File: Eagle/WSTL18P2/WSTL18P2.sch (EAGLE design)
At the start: 22 parts, among them CON1 1X6CONN-1.27-ROUND, CON2 1X6CONN-1.27-ROUND, CON3 1X6CONN-1.27-ROUND, CON4 1X6CONN-1.27-ROUND, T1 ABS07AIG

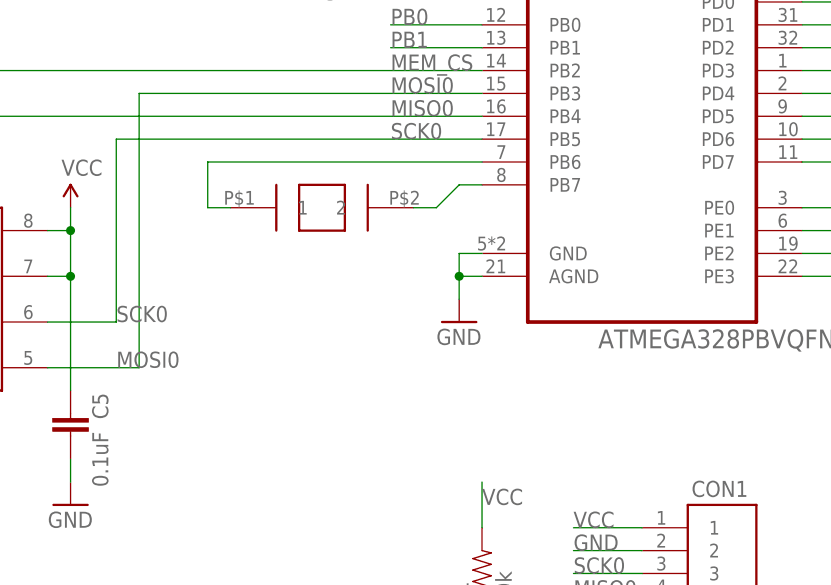
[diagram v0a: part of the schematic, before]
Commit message: Reverted some passives back to 0402 size
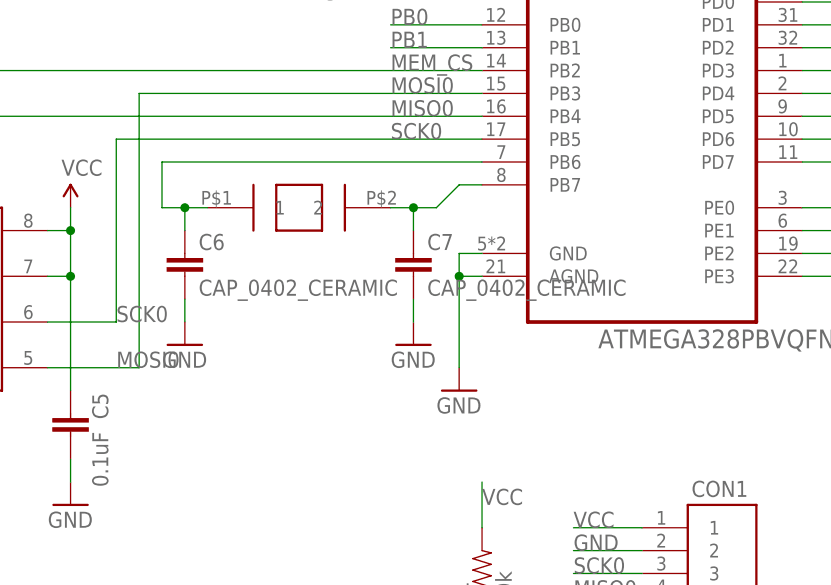
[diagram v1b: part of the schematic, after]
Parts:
- added C6, C7: CAP_0402_CERAMIC, Passives:CAP_0402_CERAMIC
- C4, C5: device Passives:CAP_0201_CERAMIC -> Passives:CAP_0402_CERAMIC
- R1, R2, R3, R4, R5: device Passives:RES_0201_CERAMIC -> Passives:RES_0402_CERAMIC
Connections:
- net GND: now also C6.2, C7.2
- net N$1: now also C7.1
- net N$2: now also C6.1
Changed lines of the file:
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@@
 <part name="GND4" library="SparkFun-Aesthetics" deviceset="GND" device=""/>
 <part name="MEM" library="Memory" deviceset="AT25DN512C-XMHF-B" device=""/>
-<part name="C4" library="Passives" deviceset="CAP_0201_CERAMIC" device="" value="0.1uF"/>
-<part name="C5" library="Passives" deviceset="CAP_0201_CERAMIC" device="" value="0.1uF"/>
+<part name="C4" library="Passives" deviceset="CAP_0402_CERAMIC" device="" value="0.1uF"/>
+<part name="C5" library="Passives" deviceset="CAP_0402_CERAMIC" device="" value="0.1uF"/>
 <part name="GND2" library="SparkFun-Aesthetics" deviceset="GND" device=""/>
 <part name="GND5" library="SparkFun-Aesthetics" deviceset="GND" device=""/>
 <part name="GND6" library="SparkFun-Aesthetics" deviceset="GND" device=""/>
 <part name="GND7" library="SparkFun-Aesthetics" deviceset="GND" device=""/>
-<part name="R2" library="Passives" deviceset="RES_0201_CERAMIC" device="" value="4.7k"/>
-<part name="R3" library="Passives" deviceset="RES_0201_CERAMIC" device="" value="4.7k"/>
-<part name="R1" library="Passives" deviceset="RES_0201_CERAMIC" device="" value="10k"/>
+<part name="R2" library="Passives" deviceset="RES_0402_CERAMIC" device="" value="4.7k"/>
+<part name="R3" library="Passives" deviceset="RES_0402_CERAMIC" device="" value="4.7k"/>
+<part name="R1" library="Passives" deviceset="RES_0402_CERAMIC" device="" value="10k"/>
 <part name="LED0" library="Passives" deviceset="LED_0402" device=""/>
 <part name="GND8" library="SparkFun-Aesthetics" deviceset="GND" device=""/>
-<part name="R5" library="Passives" deviceset="RES_0201_CERAMIC" device="" value="1k"/>
-<part name="R4" library="Passives" deviceset="RES_0201_CERAMIC" device="" value="4.7k"/>
+<part name="R5" library="Passives" deviceset="RES_0402_CERAMIC" device="" value="1k"/>
+<part name="R4" library="Passives" deviceset="RES_0402_CERAMIC" device="" value="4.7k"/>
 <part name="CON1" library="AVR_ISP_127" deviceset="1X6CONN-1.27-ROUND" device=""/>
 <part name="CON2" library="AVR_ISP_127" deviceset="1X6CONN-1.27-ROUND" device=""/>
@@
 <part name="U$1" library="Battery_holders" deviceset="LINX-CR2032-BAT-HLD-M-THM" device=""/>
 <part name="TWI" library="AVR_ISP_127" deviceset="1X2CONN1.27" device=""/>
+<part name="C6" library="Passives" deviceset="CAP_0402_CERAMIC" device=""/>
+<part name="C7" library="Passives" deviceset="CAP_0402_CERAMIC" device=""/>
+<part name="GND10" library="SparkFun-Aesthetics" deviceset="GND" device=""/>
+<part name="GND12" library="SparkFun-Aesthetics" deviceset="GND" device=""/>
 </parts>
 <sheets>
@@
 <instances>
 <instance part="MCU" gate="A" x="68.58" y="48.26"/>
-<instance part="T1" gate="G$1" x="33.02" y="27.94" smashed="yes" rot="R90"/>
+<instance part="T1" gate="G$1" x="30.48" y="27.94" smashed="yes" rot="R90"/>
 <instance part="C1" gate="G$1" x="43.18" y="71.12" smashed="yes" rot="R270">
 <attribute name="NAME" x="39.116" y="72.517" size="1.778" layer="95" align="center"/>
@@
 <instance part="GND5" gate="1" x="5.08" y="-5.08"/>
 <instance part="GND6" gate="1" x="195.58" y="45.72"/>
-<instance part="GND7" gate="1" x="48.26" y="15.24"/>
+<instance part="GND7" gate="1" x="48.26" y="7.62"/>
 <instance part="R2" gate="G$1" x="139.7" y="68.58" smashed="yes" rot="R90">
 <attribute name="NAME" x="138.2014" y="64.77" size="1.778" layer="95" rot="R90"/>
@@
 <instance part="U$1" gate="G$1" x="-76.2" y="58.42"/>
 <instance part="TWI" gate="G$1" x="127" y="78.74" rot="R90"/>
+<instance part="C6" gate="G$1" x="17.78" y="22.86"/>
+<instance part="C7" gate="G$1" x="43.18" y="22.86"/>
+<instance part="GND10" gate="1" x="43.18" y="12.7"/>
+<instance part="GND12" gate="1" x="17.78" y="12.7"/>
 </instances>
 <busses>
@@
 <pinref part="T1" gate="G$1" pin="2"/>
 <wire x1="45.72" y1="27.94" x2="43.18" y2="27.94" width="0.1524" layer="91"/>
+<pinref part="C7" gate="G$1" pin="1"/>
+<wire x1="43.18" y1="27.94" x2="40.64" y2="27.94" width="0.1524" layer="91"/>
+<wire x1="43.18" y1="25.4" x2="43.18" y2="27.94" width="0.1524" layer="91"/>
+<junction x="43.18" y="27.94"/>
 </segment>
 </net>
@@
 <pinref part="MCU" gate="A" pin="PB6"/>
 <pinref part="T1" gate="G$1" pin="1"/>
-<wire x1="50.8" y1="33.02" x2="20.32" y2="33.02" width="0.1524" layer="91"/>
-<wire x1="20.32" y1="33.02" x2="20.32" y2="27.94" width="0.1524" layer="91"/>
-<wire x1="20.32" y1="27.94" x2="22.86" y2="27.94" width="0.1524" layer="91"/>
+<wire x1="50.8" y1="33.02" x2="15.24" y2="33.02" width="0.1524" layer="91"/>
+<wire x1="15.24" y1="33.02" x2="15.24" y2="27.94" width="0.1524" layer="91"/>
+<wire x1="15.24" y1="27.94" x2="17.78" y2="27.94" width="0.1524" layer="91"/>
+<pinref part="C6" gate="G$1" pin="1"/>
+<wire x1="17.78" y1="27.94" x2="20.32" y2="27.94" width="0.1524" layer="91"/>
+<wire x1="17.78" y1="25.4" x2="17.78" y2="27.94" width="0.1524" layer="91"/>
+<junction x="17.78" y="27.94"/>
 </segment>
 </net>
@@
 <segment>
 <pinref part="GND7" gate="1" pin="GND"/>
-<wire x1="48.26" y1="17.78" x2="48.26" y2="20.32" width="0.1524" layer="91"/>
+<wire x1="48.26" y1="10.16" x2="48.26" y2="20.32" width="0.1524" layer="91"/>
 <pinref part="MCU" gate="A" pin="AGND"/>
 <wire x1="48.26" y1="20.32" x2="50.8" y2="20.32" width="0.1524" layer="91"/>
@@
 <wire x1="116.84" y1="45.72" x2="119.38" y2="45.72" width="0.1524" layer="91"/>
 </segment>
-</net>
+<segment>
+<pinref part="GND12" gate="1" pin="GND"/>
+<pinref part="C6" gate="G$1" pin="2"/>
+<wire x1="17.78" y1="15.24" x2="17.78" y2="17.78" width="0.1524" layer="91"/>
+</segment>
+<segment>
+<pinref part="GND10" gate="1" pin="GND"/>
+<pinref part="C7" gate="G$1" pin="2"/>
+<wire x1="43.18" y1="15.24" x2="43.18" y2="17.78" width="0.1524" layer="91"/>
+</segment>
+</net>

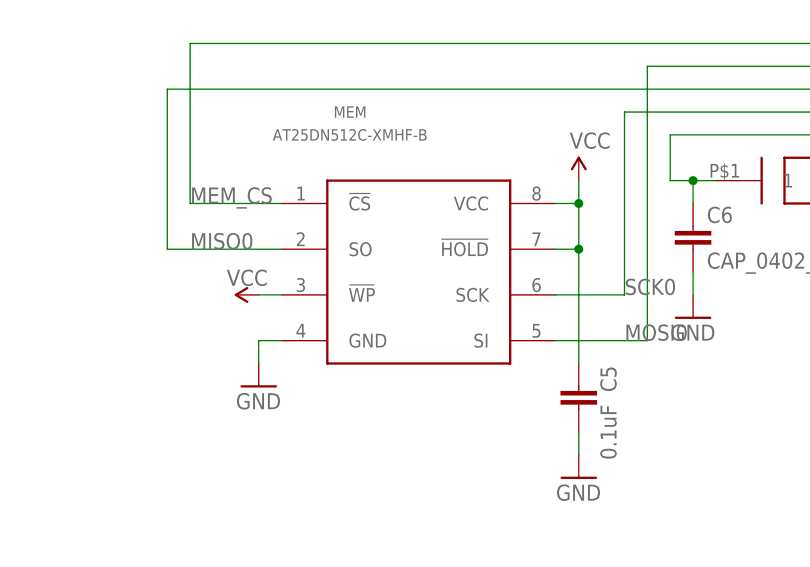
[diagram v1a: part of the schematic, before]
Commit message: Removed WP and HOLD connections to VCC on EEPROM
Chip has internal pull-ups for when WP and HOLD functions are not used
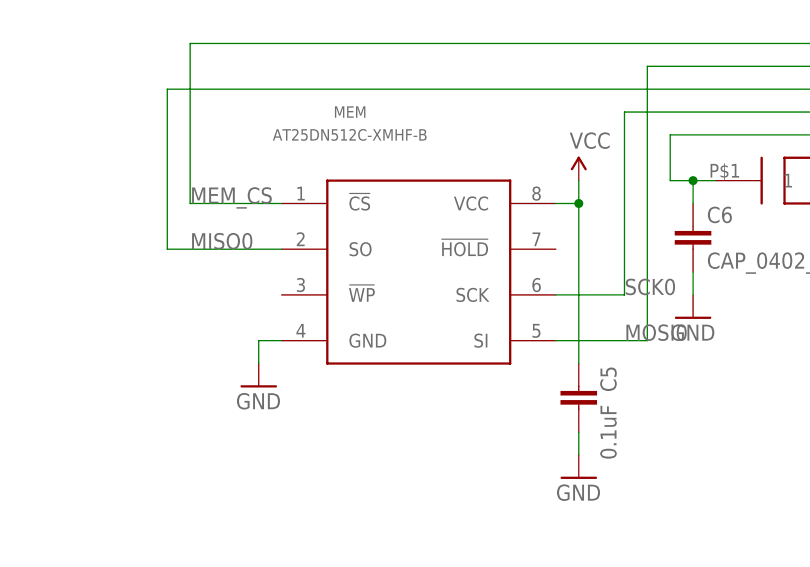
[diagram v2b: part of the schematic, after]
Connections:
- net VCC: no longer MEM.!HOLD!, MEM.!WP!
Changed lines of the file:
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@@
 <part name="GND11" library="SparkFun-Aesthetics" deviceset="GND" device=""/>
 <part name="VCC5" library="SparkFun-Aesthetics" deviceset="5V" device="" value="VCC"/>
-<part name="VCC6" library="SparkFun-Aesthetics" deviceset="5V" device="" value="VCC"/>
 <part name="VCC2" library="SparkFun-Aesthetics" deviceset="5V" device="" value="VCC"/>
 <part name="VCC3" library="SparkFun-Aesthetics" deviceset="5V" device="" value="VCC"/>
@@
 <instance part="GND11" gate="1" x="114.3" y="45.72" rot="R270"/>
 <instance part="VCC5" gate="G$1" x="5.08" y="27.94"/>
-<instance part="VCC6" gate="G$1" x="-30.48" y="15.24" smashed="yes" rot="R90">
-<attribute name="VALUE" x="-34.036" y="16.256" size="1.778" layer="96"/>
-</instance>
 <instance part="VCC2" gate="G$1" x="154.94" y="81.28"/>
 <instance part="VCC3" gate="G$1" x="147.32" y="81.28"/>
@@
 <wire x1="5.08" y1="27.94" x2="5.08" y2="25.4" width="0.1524" layer="91"/>
 <junction x="5.08" y="25.4"/>
-<pinref part="MEM" gate="G$1" pin="!HOLD!"/>
-<wire x1="2.54" y1="20.32" x2="5.08" y2="20.32" width="0.1524" layer="91"/>
-<wire x1="5.08" y1="20.32" x2="5.08" y2="25.4" width="0.1524" layer="91"/>
-<wire x1="5.08" y1="20.32" x2="5.08" y2="7.62" width="0.1524" layer="91"/>
-<junction x="5.08" y="20.32"/>
+<wire x1="5.08" y1="25.4" x2="5.08" y2="7.62" width="0.1524" layer="91"/>
 </segment>
 <segment>
-<pinref part="VCC6" gate="G$1" pin="5V"/>
-<pinref part="MEM" gate="G$1" pin="!WP!"/>
-<wire x1="-27.94" y1="15.24" x2="-30.48" y2="15.24" width="0.1524" layer="91"/>
-</segment>
-<segment>

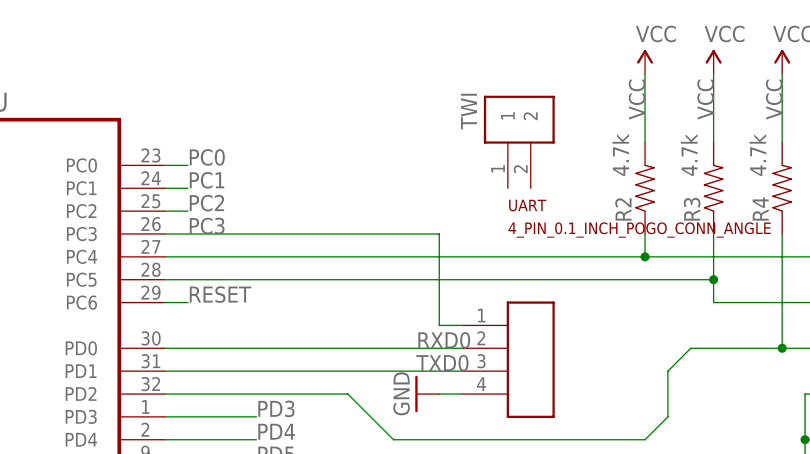
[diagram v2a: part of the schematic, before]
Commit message: Rerouted TWI (I2C)
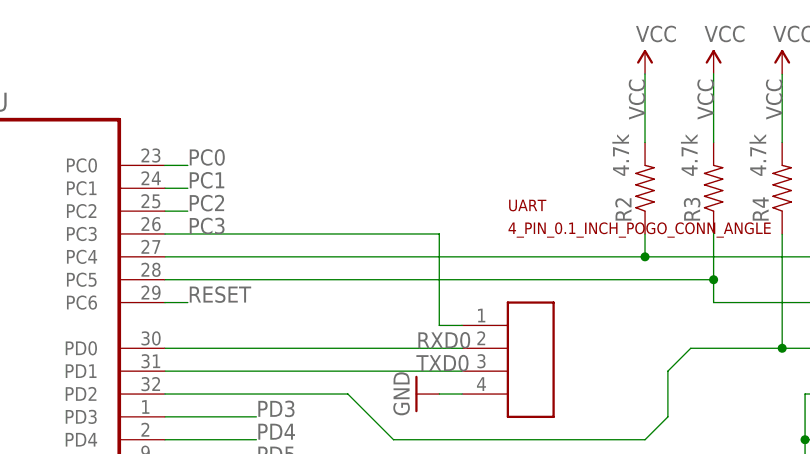
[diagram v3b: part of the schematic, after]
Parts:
- removed TWI: 1X2CONN1.27, AVR_ISP_127:1X2CONN1.27
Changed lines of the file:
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@@
 <part name="UART" library="Connectors" deviceset="4_PIN_0.1_INCH_POGO_CONN_ANGLE" device=""/>
 <part name="U$1" library="Battery_holders" deviceset="LINX-CR2032-BAT-HLD-M-THM" device=""/>
-<part name="TWI" library="AVR_ISP_127" deviceset="1X2CONN1.27" device=""/>
 <part name="C6" library="Passives" deviceset="CAP_0402_CERAMIC" device=""/>
 <part name="C7" library="Passives" deviceset="CAP_0402_CERAMIC" device=""/>
@@
 <instance part="UART" gate="G$1" x="124.46" y="48.26"/>
 <instance part="U$1" gate="G$1" x="-76.2" y="58.42"/>
-<instance part="TWI" gate="G$1" x="127" y="78.74" rot="R90"/>
 <instance part="C6" gate="G$1" x="17.78" y="22.86"/>
 <instance part="C7" gate="G$1" x="43.18" y="22.86"/>
@@
 <pinref part="R2" gate="G$1" pin="2"/>
 <wire x1="139.7" y1="63.5" x2="139.7" y2="60.96" width="0.1524" layer="91"/>
-<pinref part="MCU" gate="A" pin="PC4"/>
-<wire x1="86.36" y1="60.96" x2="139.7" y2="60.96" width="0.1524" layer="91"/>
 <pinref part="TMP" gate="G$1" pin="SDA"/>
 <wire x1="139.7" y1="60.96" x2="160.02" y2="60.96" width="0.1524" layer="91"/>
+<pinref part="MCU" gate="A" pin="PC4"/>
+<wire x1="139.7" y1="60.96" x2="86.36" y2="60.96" width="0.1524" layer="91"/>
 <junction x="139.7" y="60.96"/>
 </segment>
